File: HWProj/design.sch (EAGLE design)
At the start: 76 parts, among them IC1 LM311N, IC10 TL071P, IC11 TL071P, IC12 TL071P, IC13 TL071P, IC14 TL071P, IC15 TL071P, IC16 LM311N, IC17 TL071P, IC18 TL071P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

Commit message: silkscreen cleanup, tested square generation
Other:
- note removed: "needs testing!!"
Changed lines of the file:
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@@
 <grid distance="0.1" unitdist="inch" unit="inch" style="lines" multiple="1" display="no" altdistance="0.01" altunitdist="inch" altunit="inch"/>
 <layers>
-<layer number="1" name="Top" color="4" fill="1" visible="yes" active="no"/>
-<layer number="2" name="Route2" color="16" fill="1" visible="yes" active="no"/>
-<layer number="3" name="Route3" color="17" fill="1" visible="yes" active="no"/>
-<layer number="4" name="Route4" color="18" fill="1" visible="yes" active="no"/>
-<layer number="5" name="Route5" color="19" fill="1" visible="yes" active="no"/>
-<layer number="6" name="Route6" color="25" fill="1" visible="yes" active="no"/>
-<layer number="7" name="Route7" color="26" fill="1" visible="yes" active="no"/>
-<layer number="8" name="Route8" color="27" fill="1" visible="yes" active="no"/>
-<layer number="9" name="Route9" color="28" fill="1" visible="yes" active="no"/>
-<layer number="10" name="Route10" color="29" fill="1" visible="yes" active="no"/>
-<layer number="11" name="Route11" color="30" fill="1" visible="yes" active="no"/>
-<layer number="12" name="Route12" color="20" fill="1" visible="yes" active="no"/>
-<layer number="13" name="Route13" color="21" fill="1" visible="yes" active="no"/>
-<layer number="14" name="Route14" color="22" fill="1" visible="yes" active="no"/>
-<layer number="15" name="Route15" color="23" fill="1" visible="yes" active="no"/>
-<layer number="16" name="Bottom" color="1" fill="1" visible="yes" active="no"/>
-<layer number="17" name="Pads" color="2" fill="1" visible="yes" active="no"/>
-<layer number="18" name="Vias" color="2" fill="1" visible="yes" active="no"/>
-<layer number="19" name="Unrouted" color="6" fill="1" visible="yes" active="no"/>
-<layer number="20" name="Dimension" color="24" fill="1" visible="yes" active="no"/>
-<layer number="21" name="tPlace" color="7" fill="1" visible="yes" active="no"/>
-<layer number="22" name="bPlace" color="7" fill="1" visible="yes" active="no"/>
-<layer number="23" name="tOrigins" color="15" fill="1" visible="yes" active="no"/>
-<layer number="24" name="bOrigins" color="15" fill="1" visible="yes" active="no"/>
-<layer number="25" name="tNames" color="7" fill="1" visible="yes" active="no"/>
-<layer number="26" name="bNames" color="7" fill="1" visible="yes" active="no"/>
-<layer number="27" name="tValues" color="7" fill="1" visible="yes" active="no"/>
-<layer number="28" name="bValues" color="7" fill="1" visible="yes" active="no"/>
+<layer number="1" name="Top" color="4" fill="1" visible="no" active="no"/>
+<layer number="2" name="Route2" color="16" fill="1" visible="no" active="no"/>
+<layer number="3" name="Route3" color="17" fill="1" visible="no" active="no"/>
+<layer number="4" name="Route4" color="18" fill="1" visible="no" active="no"/>
+<layer number="5" name="Route5" color="19" fill="1" visible="no" active="no"/>
+<layer number="6" name="Route6" color="25" fill="1" visible="no" active="no"/>
+<layer number="7" name="Route7" color="26" fill="1" visible="no" active="no"/>
+<layer number="8" name="Route8" color="27" fill="1" visible="no" active="no"/>
+<layer number="9" name="Route9" color="28" fill="1" visible="no" active="no"/>
+<layer number="10" name="Route10" color="29" fill="1" visible="no" active="no"/>
+<layer number="11" name="Route11" color="30" fill="1" visible="no" active="no"/>
+<layer number="12" name="Route12" color="20" fill="1" visible="no" active="no"/>
+<layer number="13" name="Route13" color="21" fill="1" visible="no" active="no"/>
+<layer number="14" name="Route14" color="22" fill="1" visible="no" active="no"/>
+<layer number="15" name="Route15" color="23" fill="1" visible="no" active="no"/>
+<layer number="16" name="Bottom" color="1" fill="1" visible="no" active="no"/>
+<layer number="17" name="Pads" color="2" fill="1" visible="no" active="no"/>
+<layer number="18" name="Vias" color="2" fill="1" visible="no" active="no"/>
+<layer number="19" name="Unrouted" color="6" fill="1" visible="no" active="no"/>
+<layer number="20" name="Dimension" color="24" fill="1" visible="no" active="no"/>
+<layer number="21" name="tPlace" color="7" fill="1" visible="no" active="no"/>
+<layer number="22" name="bPlace" color="7" fill="1" visible="no" active="no"/>
+<layer number="23" name="tOrigins" color="15" fill="1" visible="no" active="no"/>
+<layer number="24" name="bOrigins" color="15" fill="1" visible="no" active="no"/>
+<layer number="25" name="tNames" color="7" fill="1" visible="no" active="no"/>
+<layer number="26" name="bNames" color="7" fill="1" visible="no" active="no"/>
+<layer number="27" name="tValues" color="7" fill="1" visible="no" active="no"/>
+<layer number="28" name="bValues" color="7" fill="1" visible="no" active="no"/>
 <layer number="29" name="tStop" color="7" fill="3" visible="no" active="no"/>
 <layer number="30" name="bStop" color="7" fill="6" visible="no" active="no"/>
@@
 <layer number="35" name="tGlue" color="7" fill="4" visible="no" active="no"/>
 <layer number="36" name="bGlue" color="7" fill="5" visible="no" active="no"/>
-<layer number="37" name="tTest" color="7" fill="1" visible="yes" active="no"/>
-<layer number="38" name="bTest" color="7" fill="1" visible="yes" active="no"/>
+<layer number="37" name="tTest" color="7" fill="1" visible="no" active="no"/>
+<layer number="38" name="bTest" color="7" fill="1" visible="no" active="no"/>
 <layer number="39" name="tKeepout" color="4" fill="11" visible="no" active="no"/>
 <layer number="40" name="bKeepout" color="1" fill="11" visible="no" active="no"/>
@@
 <layer number="44" name="Drills" color="7" fill="1" visible="no" active="no"/>
 <layer number="45" name="Holes" color="7" fill="1" visible="no" active="no"/>
-<layer number="46" name="Milling" color="3" fill="1" visible="yes" active="no"/>
-<layer number="47" name="Measures" color="7" fill="1" visible="yes" active="no"/>
-<layer number="48" name="Document" color="7" fill="1" visible="yes" active="no"/>
-<layer number="49" name="Reference" color="7" fill="1" visible="yes" active="no"/>
-<layer number="50" name="dxf" color="7" fill="1" visible="yes" active="no"/>
-<layer number="51" name="tDocu" color="7" fill="1" visible="yes" active="no"/>
-<layer number="52" name="bDocu" color="7" fill="1" visible="yes" active="no"/>
-<layer number="53" name="tGND_GNDA" color="7" fill="9" visible="yes" active="no"/>
-<layer number="54" name="bGND_GNDA" color="1" fill="9" visible="yes" active="no"/>
-<layer number="56" name="wert" color="7" fill="1" visible="yes" active="no"/>
-<layer number="57" name="tCAD" color="7" fill="1" visible="yes" active="no"/>
-<layer number="59" name="tCarbon" color="7" fill="1" visible="yes" active="no"/>
-<layer number="60" name="bCarbon" color="7" fill="1" visible="yes" active="no"/>
-<layer number="62" name="Desc" color="7" fill="1" visible="yes" active="no"/>
+<layer number="46" name="Milling" color="3" fill="1" visible="no" active="no"/>
+<layer number="47" name="Measures" color="7" fill="1" visible="no" active="no"/>
+<layer number="48" name="Document" color="7" fill="1" visible="no" active="no"/>
+<layer number="49" name="Reference" color="7" fill="1" visible="no" active="no"/>
+<layer number="50" name="dxf" color="7" fill="1" visible="no" active="no"/>
+<layer number="51" name="tDocu" color="7" fill="1" visible="no" active="no"/>
+<layer number="52" name="bDocu" color="7" fill="1" visible="no" active="no"/>
+<layer number="53" name="tGND_GNDA" color="7" fill="9" visible="no" active="no"/>
+<layer number="54" name="bGND_GNDA" color="1" fill="9" visible="no" active="no"/>
+<layer number="56" name="wert" color="7" fill="1" visible="no" active="no"/>
+<layer number="57" name="tCAD" color="7" fill="1" visible="no" active="no"/>
+<layer number="59" name="tCarbon" color="7" fill="1" visible="no" active="no"/>
+<layer number="60" name="bCarbon" color="7" fill="1" visible="no" active="no"/>
+<layer number="62" name="Desc" color="7" fill="1" visible="no" active="no"/>
 <layer number="88" name="SimResults" color="9" fill="1" visible="yes" active="yes"/>
 <layer number="89" name="SimProbes" color="9" fill="1" visible="yes" active="yes"/>
@@
 <text x="266.7" y="88.9" size="1.778" layer="150">inverted external outputs!!</text>
 <text x="281.94" y="58.42" size="1.778" layer="94" rot="R180">3.5mm jack</text>
-<text x="198.12" y="27.94" size="1.778" layer="150">needs testing!!</text>
 <text x="256.54" y="269.24" size="1.778" layer="94" rot="R180">1</text>
 <text x="256.54" y="243.84" size="1.778" layer="94" rot="R180">2</text>

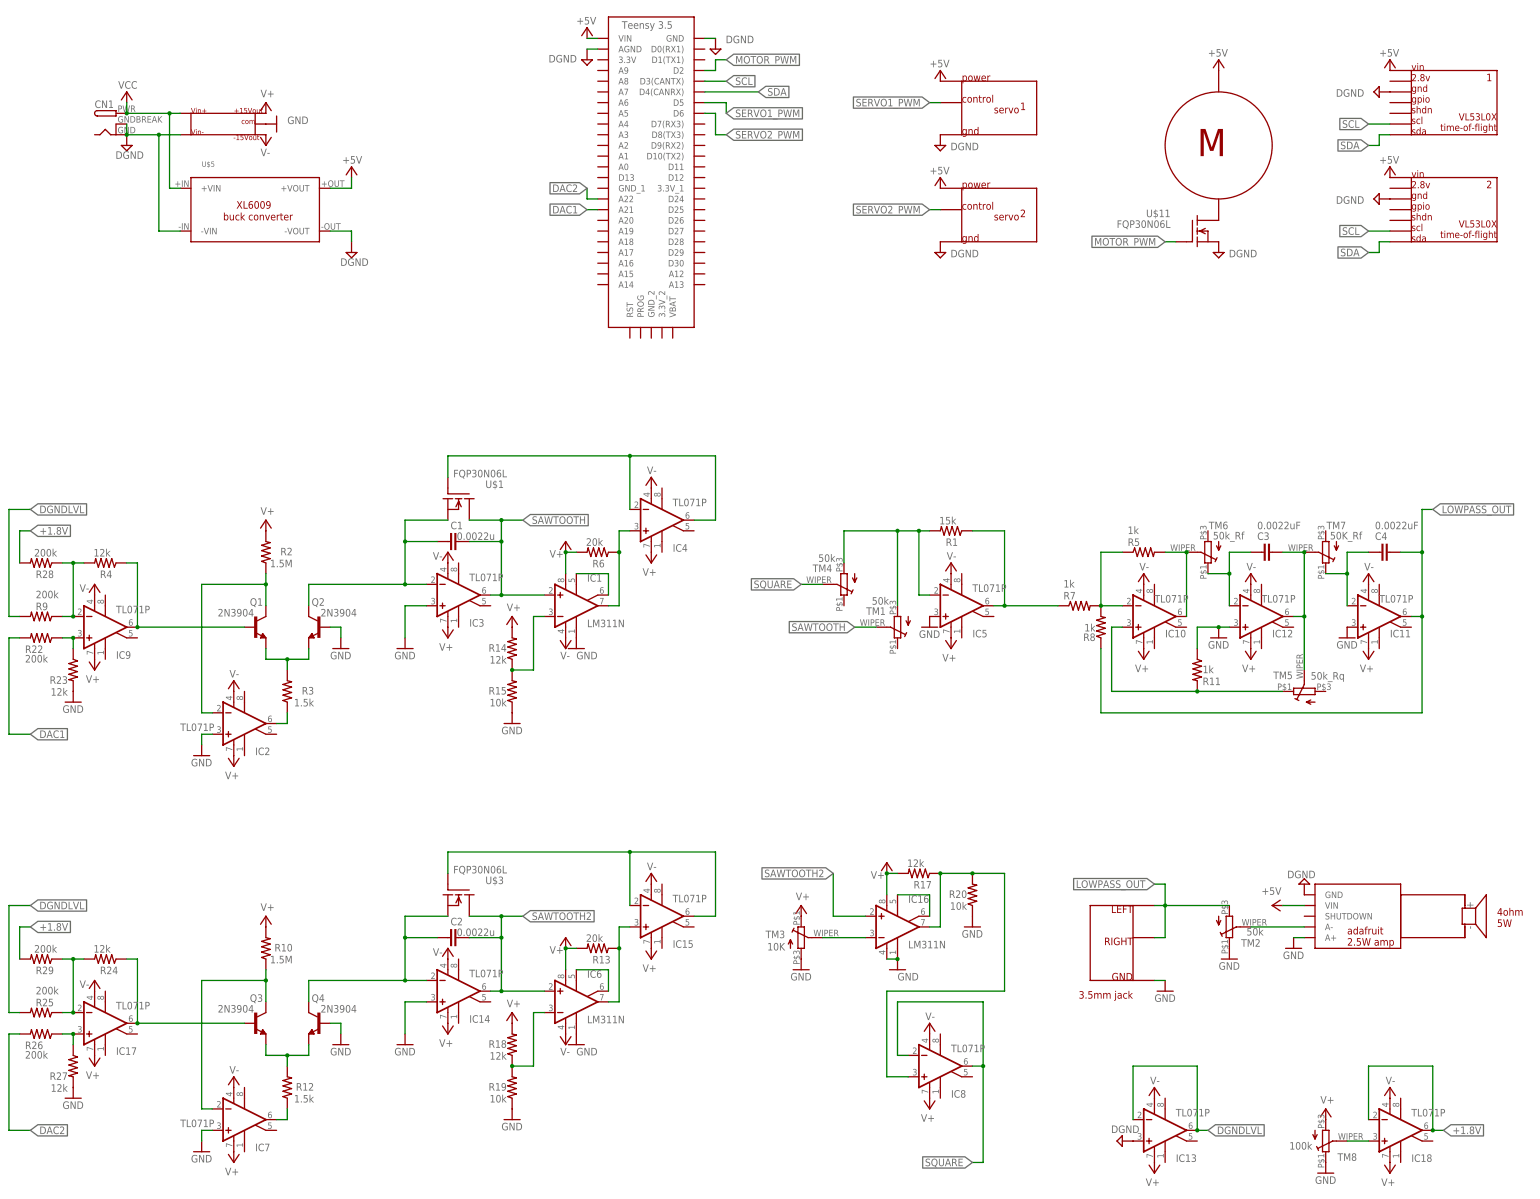
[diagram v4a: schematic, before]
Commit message: added fuses, shunt system, finalized board rev1.1
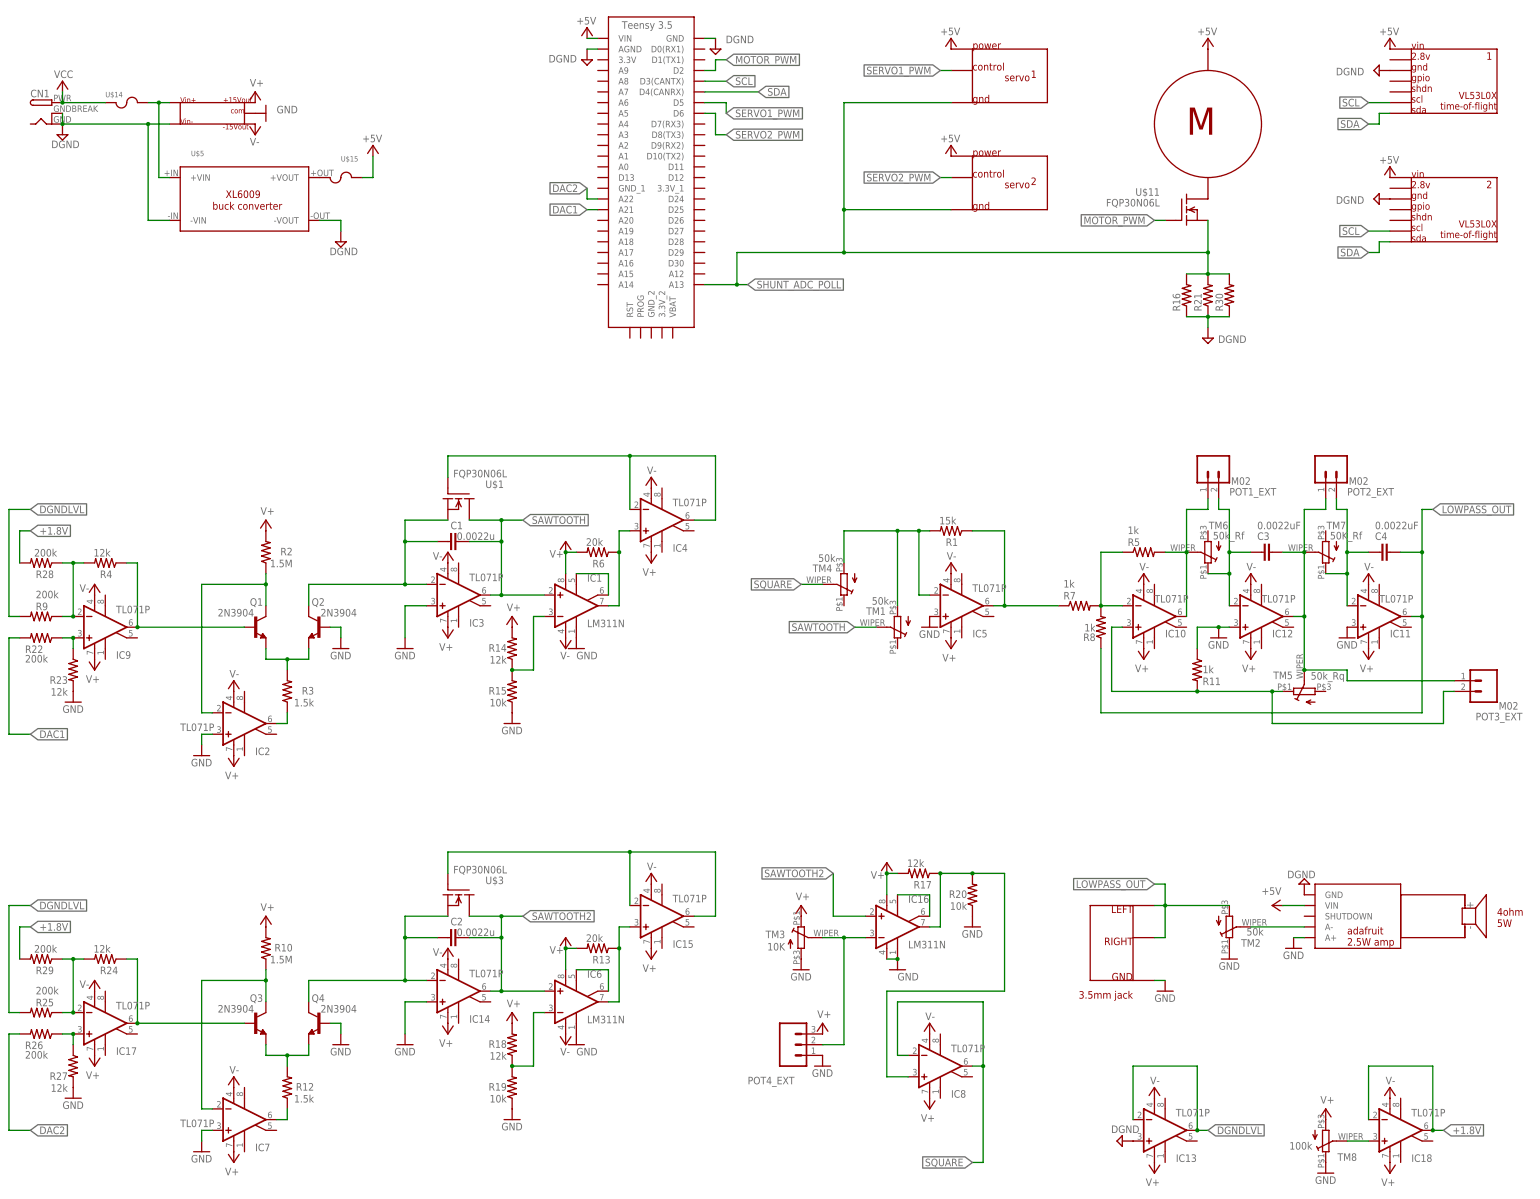
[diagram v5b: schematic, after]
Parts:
- added POT1_EXT, POT2_EXT, POT3_EXT: M02, HyTechDevices:M02
- added POT4_EXT: (no value), HyTechDevices:M03
- added R16, R21, R30: (no value), HyTechDevices:RESISTORAXIAL-0.3
- added U$14, U$15: (no value), HyTechDevices:FUSE_5X20MM
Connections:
- new net N$29: U$14.2, U$5.+VIN, U$7.2
- new net N$32: U$15.1, U$5.+VOUT
- new net SHUNT_ADC_POLL: R16.2, R21.2, R30.2, U$11.S, U$4.A13, U$8.GND, U$9.GND
- net +5V: now also U$15.2; no longer U$5.+VOUT
- net BANDPASS_OUT: now also POT2_EXT.1, POT3_EXT.1
- net DGND: now also R16.1, R21.1, R30.1; no longer U$11.S, U$8.GND, U$9.GND
- net GND: now also POT4_EXT.1
- net HIGHPASS_OUT: now also POT1_EXT.1
- net N$20: now also POT1_EXT.2
- net N$22: now also POT2_EXT.2
- net N$25: now also POT3_EXT.2
- net N$26: now also POT4_EXT.2
- net V+: now also POT4_EXT.3
- net VCC: now also U$14.1; no longer U$5.+VIN, U$7.2
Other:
- note added: "1.5-2A slow-blow"
- note added: "1ohm all"
- note added: "2A slow-blow"
- note added: "shunt resistors"
- moved on the sheet: CN1, U$11, U$5

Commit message: attempted integration of buttons and servos
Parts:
- added LED, PAUSE, PLAY, POWER, REC: M02, HyTechDevices:M02
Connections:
- net +1.8V renamed +1.7V
- new net LED: LED.2, U$4.D0(RX1)
- new net PAUSE: PAUSE.2, U$4.A16
- new net PLAY: PLAY.2, U$4.A15
- new net POWER: POWER.2, U$4.A14
- new net RECORD: REC.2, U$4.A17
- net DGND: now also LED.1, PAUSE.1, PLAY.1, POWER.1, REC.1
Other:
- note added: "button connections"
- moved on the sheet: CN1, R16, R21, R30, U$11, U$14, U$15, U$5
